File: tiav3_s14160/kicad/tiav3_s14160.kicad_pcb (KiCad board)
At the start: 4 copper layers, 25.3 x 25.3 mm, 22 parts, among them J1 SSQ-103-01-G-D, J2 Conn_Coaxial, U1 OPA847IDBVT

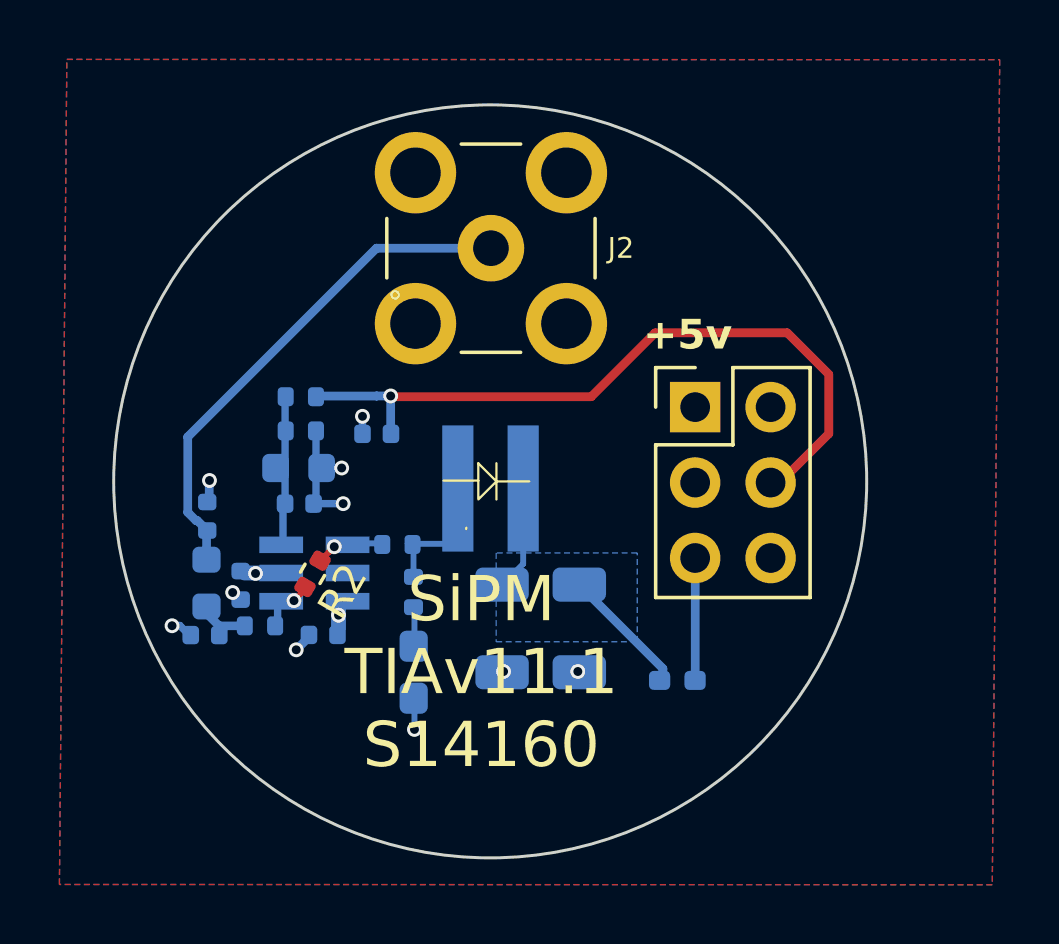
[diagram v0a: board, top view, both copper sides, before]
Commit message: Update KiCad designs for all 3 boards and re-export gerbers
- bias-control-lt8362: schematic + PCB updates, exported gerbers
  including new B_Paste/F_Paste layers
- power-supply: schematic + PCB updates, re-exported gerbers with new
  naming (.gbl/.gbs/.gto/.gtl/.gts) replacing old .gbr files, added
  paste layer exports
- tiav3_s14160: schematic + PCB updates, re-exported gerbers with new
  naming, added paste layer exports
- fp-lib-table updates across all four board projects
- new "w paste" gerber zip exports for assembly
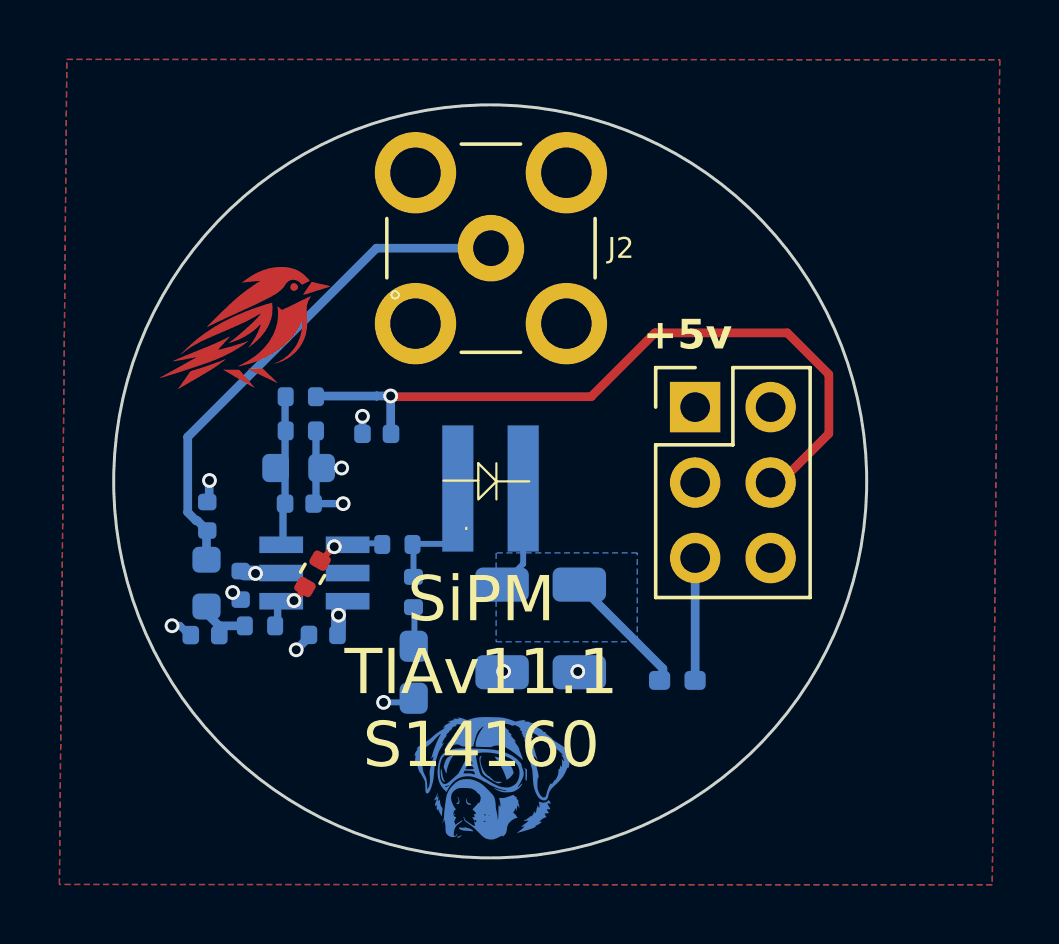
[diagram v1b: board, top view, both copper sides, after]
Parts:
- added J3: Snibbor Inc LOGO, snibbor_logos:snibbor_inc_logo, F.Cu at (191.3, 93.1)
- added J4: Bennett close LOGO, snibbor_logos:Bennett logo close 1 layered, B.Cu at (199.6, 108.8)
